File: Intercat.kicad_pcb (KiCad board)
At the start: 2 copper layers, 80 x 38 mm, 83 parts, among them J3 DE9_Receptacle, J4 USB_C_Receptacle_USB2.0, T1 LM-NP-1001-B1L, T4 LM-NP-1001-B1L, U1 CP2615-xx-xM, U10 MAX3250, U11 EL357N(C)(TA)-G, U12 EL357N(C)(TA)-G, U2 USBLC6-2SC6, U3 PCM3060, U4 MCP6002, U6 MCP6002, U8 EL357N(C)(TA)-G, U9 EL357N(C)(TA)-G

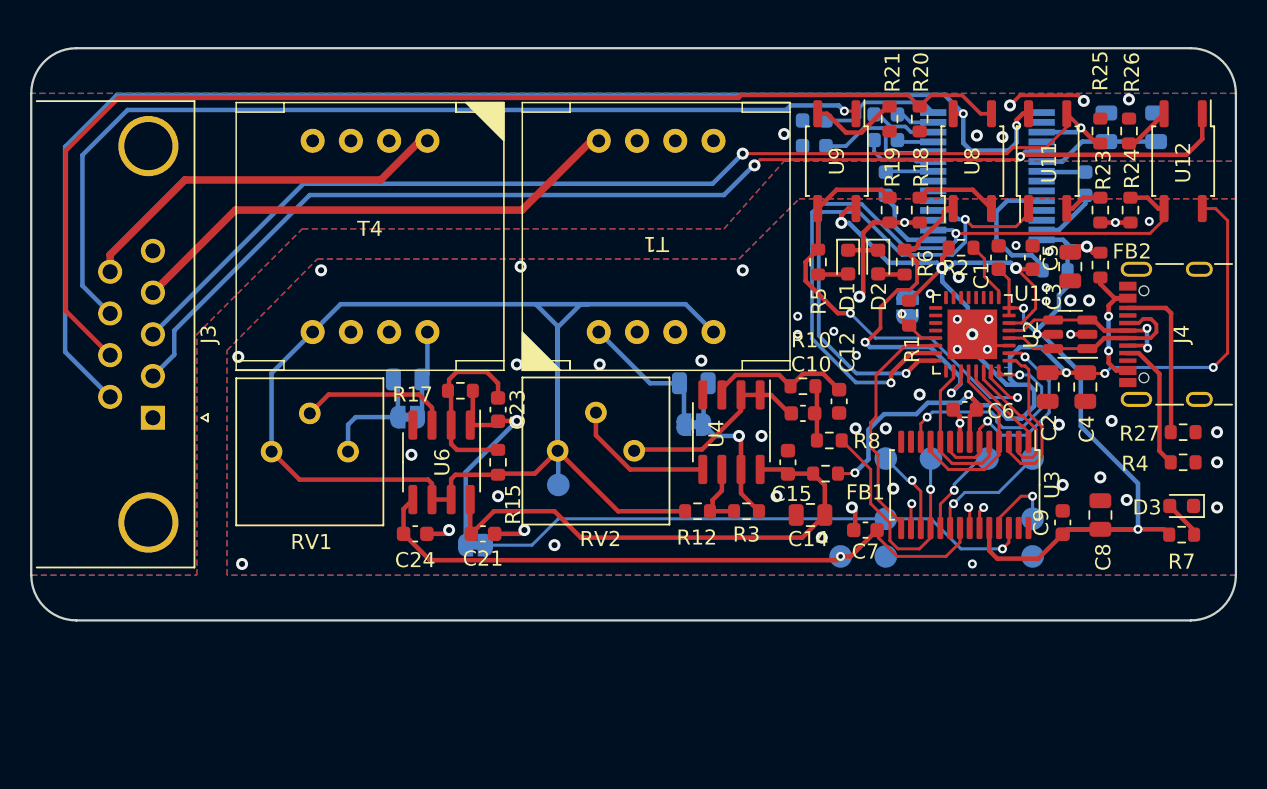
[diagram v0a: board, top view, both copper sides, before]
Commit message: little pcb modification and silkscreen
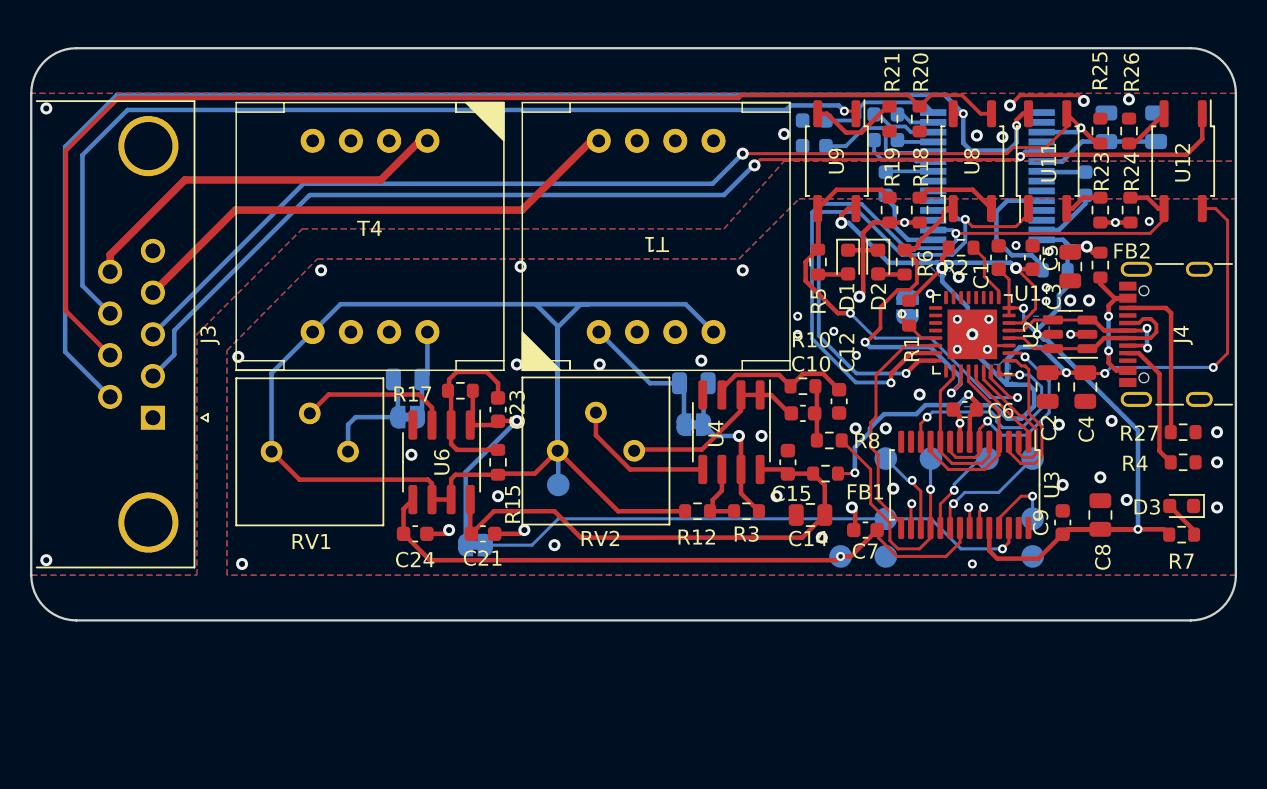
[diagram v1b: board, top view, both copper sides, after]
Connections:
- J3 pad 0: (no net) -> GNDA
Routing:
- net GNDA: vias 6 -> 8
- added copper zone on B.Cu, net VBUS
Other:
- board text added: "IU2RRT"
- board text added: "XZ Group"

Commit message: little pcb modification
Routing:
- net VBUS: track 58.2 -> 59.4 mm
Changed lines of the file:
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@@
   (segment (start 169.2 75.175) (end 169.15 75.175) (width 0.25) (layer "B.Cu") (net 1))
   (segment (start 169.2 75.175) (end 168.975 75.175) (width 0.3) (layer "B.Cu") (net 1))
-  (segment (start 166.9 81) (end 167.25 81.35) (width 0.3) (layer "B.Cu") (net 1))
   (segment (start 168.25 79.25) (end 168.25 78.4) (width 0.3) (layer "B.Cu") (net 1))
-  (segment (start 167.25 81.35) (end 167.469239 81.35) (width 0.3) (layer "B.Cu") (net 1))
   (segment (start 168.825 77.825) (end 168.25 78.4) (width 0.3) (layer "B.Cu") (net 1))
+  (segment (start 169.7 83.58076) (end 167.469239 81.35) (width 0.3) (layer "B.Cu") (net 1))
+  (segment (start 167.25 81.35) (end 166.9 81) (width 0.3) (layer "B.Cu") (net 1))
   (segment (start 168.825 76.75) (end 168.825 77.825) (width 0.3) (layer "B.Cu") (net 1))
   (segment (start 166.8 81) (end 166.8 80.7) (width 0.3) (layer "B.Cu") (net 1))
-  (segment (start 166.8 81) (end 166.9 81) (width 0.3) (layer "B.Cu") (net 1))
   (segment (start 168.825 75.5) (end 168.825 76.75) (width 0.3) (layer "B.Cu") (net 1))
+  (segment (start 167.469239 81.35) (end 167.25 81.35) (width 0.3) (layer "B.Cu") (net 1))
   (segment (start 165.9005 79.268981) (end 165.9005 80.1005) (width 0.2) (layer "B.Cu") (net 1))
+  (segment (start 173.5 93.95) (end 173.5 87.380761) (width 0.3) (layer "B.Cu") (net 1))
   (segment (start 168.7 74.9) (end 168.825 75.025) (width 0.3) (layer "B.Cu") (net 1))
+  (segment (start 170.04038 85.84038) (end 169.7 85.5) (width 0.3) (layer "B.Cu") (net 1))
   (segment (start 168.525 74.725) (end 168.7 74.9) (width 0.3) (layer "B.Cu") (net 1))
   (segment (start 165.9005 80.1005) (end 166.8 81) (width 0.2) (layer "B.Cu") (net 1))
-  (segment (start 173.5 87.380761) (end 173.5 93.95) (width 0.3) (layer "B.Cu") (net 1))
   (segment (start 168.975 75.175) (end 168.7 74.9) (width 0.3) (layer "B.Cu") (net 1))
+  (segment (start 173.5 87.380761) (end 171.95962 85.84038) (width 0.3) (layer "B.Cu") (net 1))
   (segment (start 170.1 75.175) (end 169.2 75.175) (width 0.3) (layer "B.Cu") (net 1))
   (segment (start 167.1 74.725) (end 168.525 74.725) (width 0.3) (layer "B.Cu") (net 1))
   (segment (start 166.8 80.7) (end 168.25 79.25) (width 0.3) (layer "B.Cu") (net 1))
   (segment (start 168.825 75.025) (end 168.825 75.5) (width 0.3) (layer "B.Cu") (net 1))
-  (segment (start 167.469239 81.35) (end 173.5 87.380761) (width 0.3) (layer "B.Cu") (net 1))
+  (segment (start 171.95962 85.84038) (end 170.04038 85.84038) (width 0.3) (layer "B.Cu") (net 1))
+  (segment (start 169.7 85.5) (end 169.7 83.58076) (width 0.3) (layer "B.Cu") (net 1))
   (segment (start 169.15 75.175) (end 168.825 75.5) (width 0.25) (layer "B.Cu") (net 1))
+  (segment (start 166.9 81) (end 166.8 81) (width 0.3) (layer "B.Cu") (net 1))
   (segment (start 130.775 94.25) (end 132.5 94.25) (width 0.3) (layer "F.Cu") (net 2))
   (segment (start 155.925 73.575) (end 157 73.575) (width 0.3) (layer "F.Cu") (net 2))
@@
   (segment (start 154.1 67.6) (end 152.85 66.35) (width 0.3) (layer "F.Cu") (net 39))
   (segment (start 152.85 66.35) (end 152.23 66.35) (width 0.3) (layer "F.Cu") (net 39))
-  (segment (start 166.45 75.75) (end 165.130761 75.75) (width 0.3) (layer "B.Cu") (net 40))
+  (segment (start 167.175 76.75) (end 166.35 76.75) (width 0.3) (layer "B.Cu") (net 40))
+  (segment (start 164.1 72.85) (end 164.825 72.125) (width 0.3) (layer "B.Cu") (net 40))
+  (segment (start 165.130761 75.75) (end 164.1 74.719239) (width 0.3) (layer "B.Cu") (net 40))
   (segment (start 164.1 74.719239) (end 164.1 72.85) (width 0.3) (layer "B.Cu") (net 40))
-  (segment (start 165.130761 75.75) (end 164.1 74.719239) (width 0.3) (layer "B.Cu") (net 40))
-  (segment (start 167.175 76.475) (end 166.45 75.75) (width 0.3) (layer "B.Cu") (net 40))
-  (segment (start 164.1 72.85) (end 164.825 72.125) (width 0.3) (layer "B.Cu") (net 40))
-  (segment (start 167.175 76.75) (end 167.175 76.475) (width 0.3) (layer "B.Cu") (net 40))
+  (segment (start 166.35 76.75) (end 166.15 76.55) (width 0.3) (layer "B.Cu") (net 40))
   (segment (start 164.825 72.125) (end 167.1 72.125) (width 0.3) (layer "B.Cu") (net 40))
+  (segment (start 165.610661 75.75) (end 165.130761 75.75) (width 0.3) (layer "B.Cu") (net 40))
+  (segment (start 166.15 76.289339) (end 165.610661 75.75) (width 0.3) (layer "B.Cu") (net 40))
+  (segment (start 166.15 76.55) (end 166.15 76.289339) (width 0.3) (layer "B.Cu") (net 40))
   (segment (start 175.35 79.25) (end 175.7 79.6) (width 0.3) (layer "F.Cu") (net 41))
   (segment (start 175.7 79.6) (end 175.7 87.475) (width 0.3) (layer "F.Cu") (net 41))

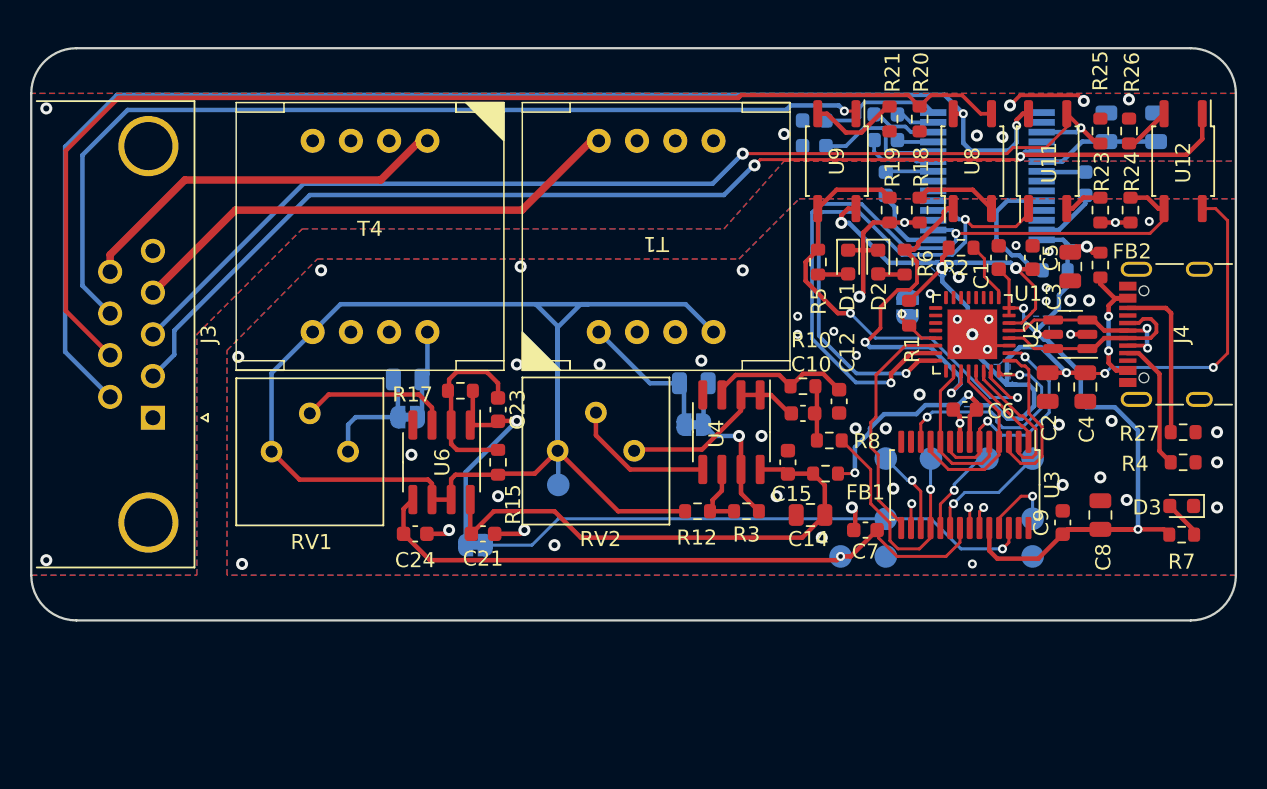
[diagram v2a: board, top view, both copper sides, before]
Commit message: modified silkscreen
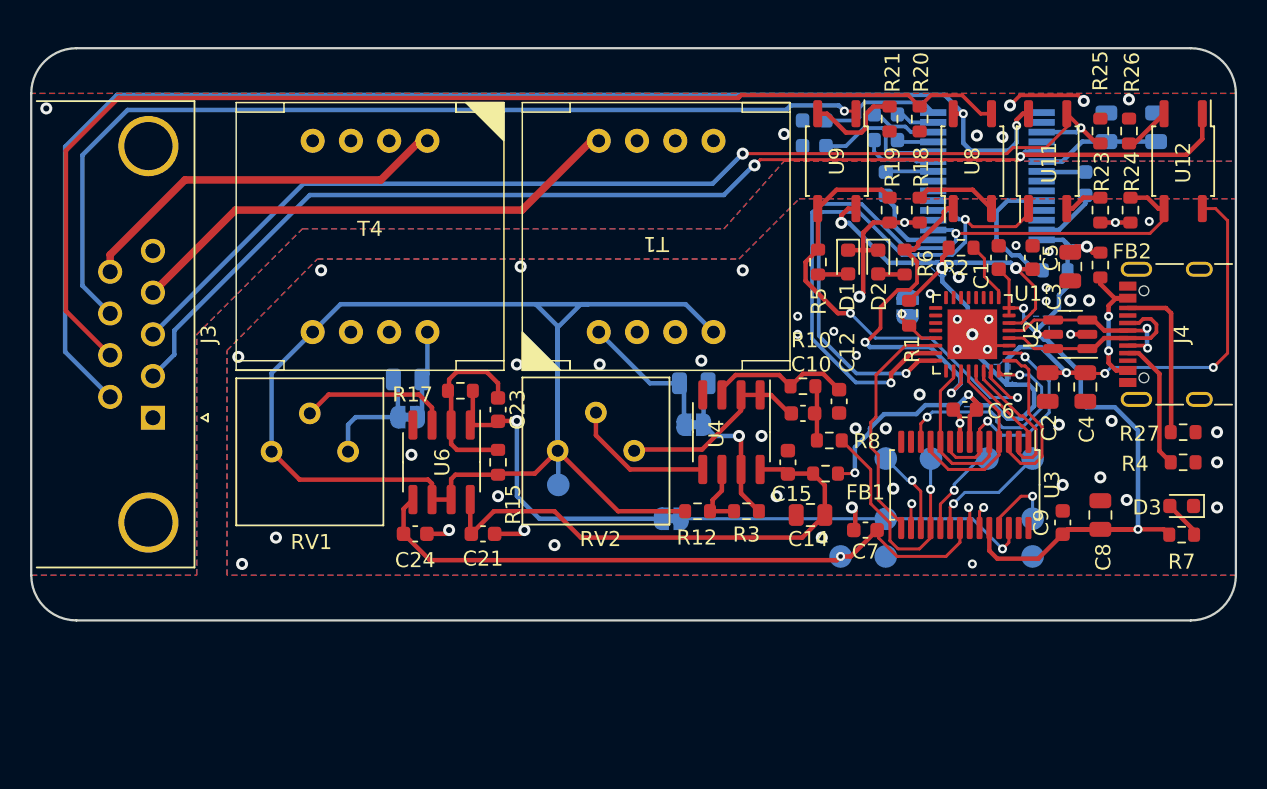
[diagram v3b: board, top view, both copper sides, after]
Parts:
- moved JP2 13.1 mm to (142.5, 93.2)
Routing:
- net /ADC_Rin: track 37.5 -> 23.7 mm
- net Net-(JP2-A): track 15.2 -> 20.8 mm
- net Net-(R21-Pad2): track 6.00 -> 6.55 mm
- net GNDA: vias 8 -> 7
- net GND: vias 56 -> 57
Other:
- board text added: "CTS"
- board text added: "DESIGNED BY THE AMABILE IU2RRT"
- board text added: "GND"
- board text added: "IN"
- board text added: "L"
- board text added: "L+"
- board text added: "L-"
- board text added: "OUT"
- board text added: "R"
- board text added: "R+"
- board text added: "R-"
- board text added: "RTS"
- board text added: "RX"
- board text added: "TX"
- board text added: "VCC"
- board text added: "VREF"
- board text added: "VREF#"
- board text added: "XENOM NOT INCLUDED"
- board text removed: "IU2RRT"
- board text removed: "XZ Group"

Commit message: Started work on the PBClayout of the new version
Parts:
- added C16: 1u, Capacitor_SMD:C_0805_2012Metric, F.Cu at (149.1, 88.9)
- added R9: 4k7, Resistor_SMD:R_0603_1608Metric, F.Cu at (148.8, 96.0)
- added U5: AMS1117-3.3, Package_TO_SOT_SMD:SOT-223-3_TabPin2, F.Cu at (174.8, 92.5)
- C2, C4: value 1u -> 100n; footprint Capacitor_SMD:C_0805_2012Metric -> Capacitor_SMD:C_0603_1608Metric
- C6: value 100n -> 1u; footprint Capacitor_SMD:C_0603_1608Metric -> Capacitor_SMD:C_0805_2012Metric
- U1: value CP2615-xx-xM -> STM32F072CBTx; footprint Package_DFN_QFN:QFN-32-1EP_5x5mm_P0.5mm_EP3.3x3.3mm -> Package_QFP:LQFP-48_7x7mm_P0.5mm
- moved C12 29.7 mm to (124.0, 85.4), turned to 90 degrees
- moved JP4 29.2 mm to (114.8, 85.6), turned to 0 degrees
- moved C13 26.9 mm to (117.1, 82.8), turned to 0 degrees
- moved R10 25.8 mm to (125.5, 85.4), turned to -90 degrees
- moved R8 24.6 mm to (128.5, 85.4), turned to 90 degrees
- moved C10 24.3 mm to (127.0, 85.4), turned to 90 degrees
- moved C8 22.7 mm to (148.3, 91.9)
- moved R12 22.5 mm to (121.9, 95.5)
- moved R3 21.7 mm to (126.0, 95.5)
- moved C15 21.6 mm to (129.5, 95.5), turned to 0 degrees
- moved U4 20.6 mm to (126.2, 90.9)
- moved C9 19.7 mm to (148.8, 94.5), turned to 180 degrees
- moved RV2 19.6 mm to (120.4, 88.4)
- moved TP1 19.6 mm to (115.4, 90.5)
- moved T1 19.6 mm to (121.9, 74.2)
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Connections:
- C1 pad 1: VBUS -> +3.3V
- C14 pad 2: VDDA -> +3.3V
- C15 pad 1: VDDA -> +5V
- C2 pad 1: GND -> +3.3V
- C2 pad 2: VDD -> GND
- C21 pad 1: VDDA -> +5V
- C4 pad 1: GND -> +3.3V
- C4 pad 2: VDD -> GND
- C5 pad 1: VDD -> +3.3V
- C6 pad 1: VDD -> GND
- C6 pad 2: GND -> VBUS
- C7 pad 1: /DAC_Vref -> +3.3V
- C8 pad 2: VBUS -> +5V
- C9 pad 1: VBUS -> +5V
- FB1 pad 1: VDD -> VBUS
- FB1 pad 2: VDDA -> +5V
- FB2 pad 1: Net-(FB2-Pad1) -> /VBUS#
- J3 pad 0: GNDA -> (no net)
- J4 pad A4: Net-(FB2-Pad1) -> /VBUS#
- J4 pad A9: Net-(FB2-Pad1) -> /VBUS#
- J4 pad B4: Net-(FB2-Pad1) -> /VBUS#
- J4 pad B9: Net-(FB2-Pad1) -> /VBUS#
- JP2 pad 2: /ADC_Rin -> /ADC_Lin
- R1 pad 1: Net-(JP1-B) -> Net-(U1-BOOT0)
- R1 pad 2: VDD -> +3.3V
- R2 pad 1: Net-(U1-~{RST}) -> Net-(U1-NRST)
- R2 pad 2: VDD -> +3.3V
- R5 pad 1: /CTS -> /LED2
- R6 pad 1: /RTS -> /LED1
- R7 pad 1: VBUS -> /LED0
- R8 pad 1: /DAC_Rout -> /DAC_Lout
- U1 pad 1: /DIN -> +3.3V
- U1 pad 10: unconnected-(U1-NC-Pad10) -> /CTS
- U1 pad 11: unconnected-(U1-GPIO.7-Pad11) -> /RTS
- U1 pad 12: unconnected-(U1-GPIO.6-Pad12) -> /TX
- U1 pad 13: unconnected-(U1-GPIO.5-Pad13) -> /RX
- U1 pad 14: unconnected-(U1-GPIO.4-Pad14) -> /I2S_WS1
- U1 pad 15: unconnected-(U1-GPIO.3-Pad15) -> /I2S_CK1
- U1 pad 16: unconnected-(U1-GPIO.2-Pad16) -> /MCLK
- U1 pad 17: unconnected-(U1-GPIO.1-Pad17) -> /I2S_SD1
- U1 pad 18: unconnected-(U1-GPIO.0-Pad18) -> /LED0
- U1 pad 19: unconnected-(U1-GPIO.9/BUTTONS-Pad19) -> /LED1
- U1 pad 2: /SCLK -> unconnected-(U1-PC13-Pad2)
- U1 pad 20: unconnected-(U1-GPIO.8/ADC-Pad20) -> /LED2
- U1 pad 21: Net-(JP1-B) -> /I2S_CK2
- U1 pad 22: /RESET_OUT -> unconnected-(U1-PB11-Pad22)
- U1 pad 23: /RX -> GND
- U1 pad 24: /TX -> +3.3V
- U1 pad 25: unconnected-(U1-GPIO.12/CLKOUT-Pad25) -> /I2S_WS2
- U1 pad 26: /MCLK -> unconnected-(U1-PB13-Pad26)
- U1 pad 27: /RTS -> unconnected-(U1-PB14-Pad27)
- U1 pad 28: /LRCLK -> /I2S_SD2
- U1 pad 29: /SCL -> unconnected-(U1-PA8-Pad29)
- U1 pad 3: GND -> unconnected-(U1-PC14-Pad3)
- U1 pad 30: /SDA -> unconnected-(U1-PA9-Pad30)
- U1 pad 31: /CTS -> unconnected-(U1-PA10-Pad31)
- U1 pad 32: /DOUT -> /D-
- U1 pad 33: GND -> /D+
- U1 pad 4: /D+ -> unconnected-(U1-PC15-Pad4)
- U1 pad 5: /D- -> /OSCIN
- U1 pad 6: VDD -> /OSCOUT
- U1 pad 7: VBUS -> Net-(U1-NRST)
- U1 pad 8: VBUS -> GND
- U1 pad 9: Net-(U1-~{RST}) -> +3.3V
- U12 pad 6: VDD -> +3.3V
- U2 pad 5: VBUS -> /VBUS#
- U3 pad 10: /MCLK -> /I2S_CK2
- U3 pad 11: /LRCLK -> /I2S_WS2
- U3 pad 12: /DOUT -> /I2S_SD2
- U3 pad 15: /RESET_OUT -> /RESET_DAC
- U3 pad 24: VBUS -> +5V
- U3 pad 27: unconnected-(U3-nMS-Pad27) -> Net-(JP1-B)
- U3 pad 28: unconnected-(U3-MODE-Pad28) -> GND
- U3 pad 3: /DIN -> /I2S_SD1
- U3 pad 4: /LRCLK -> /I2S_WS1
- U3 pad 5: /MCLK -> /I2S_CK1
- U3 pad 6: /SCLK -> /MCLK
- U3 pad 7: VDD -> +3.3V
- U3 pad 9: /SCLK -> /MCLK
- U4 pad 8: VDDA -> +5V
- U6 pad 8: VDDA -> +5V
- U9 pad 6: VDD -> +3.3V
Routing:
- net VDD: track 90.4 -> 0.00 mm, vias 8 -> 0
- net VS: track 88.5 -> 0.00 mm, vias 2 -> 0
- net /RTS_ISO: track 78.9 -> 5.96 mm
- net /CTS_ISO: track 64.2 -> 0.00 mm, vias 1 -> 0
- net /RX_ISO: track 80.3 -> 37.4 mm
- net VBUS: track 59.4 -> 23.0 mm, vias 4 -> 2
- net VDDA: track 34.5 -> 0.00 mm
- net GND: track 29.1 -> 2.66 mm, vias 57 -> 0
- net /ADC_Rin: track 23.7 -> 0.00 mm, vias 1 -> 0
- net +3.3V: track 0.00 -> 23.7 mm
- net /DAC_Vref: track 43.4 -> 21.3 mm, vias 1 -> 0
- net /Analog Filter/Vref#: track 93.9 -> 72.0 mm, vias 0 -> 1
- net /DAC_Lout: track 8.20 -> 29.9 mm, vias 1 -> 2
- net /OUT_ISO: track 34.0 -> 14.6 mm
- net /RX: track 49.7 -> 31.0 mm
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- removed copper zone on B.Cu, net /Analog Filter/Vref#
- removed copper zone on B.Cu, net VBUS
- removed copper zone on B.Cu, net VDD
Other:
- copper layers 2 -> 4
